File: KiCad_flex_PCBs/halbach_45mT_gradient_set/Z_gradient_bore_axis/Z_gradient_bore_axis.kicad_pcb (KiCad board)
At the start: 2 copper layers, 209.7 x 123 mm, 70 parts, among them J1+ SolderPad, J2- SolderPad

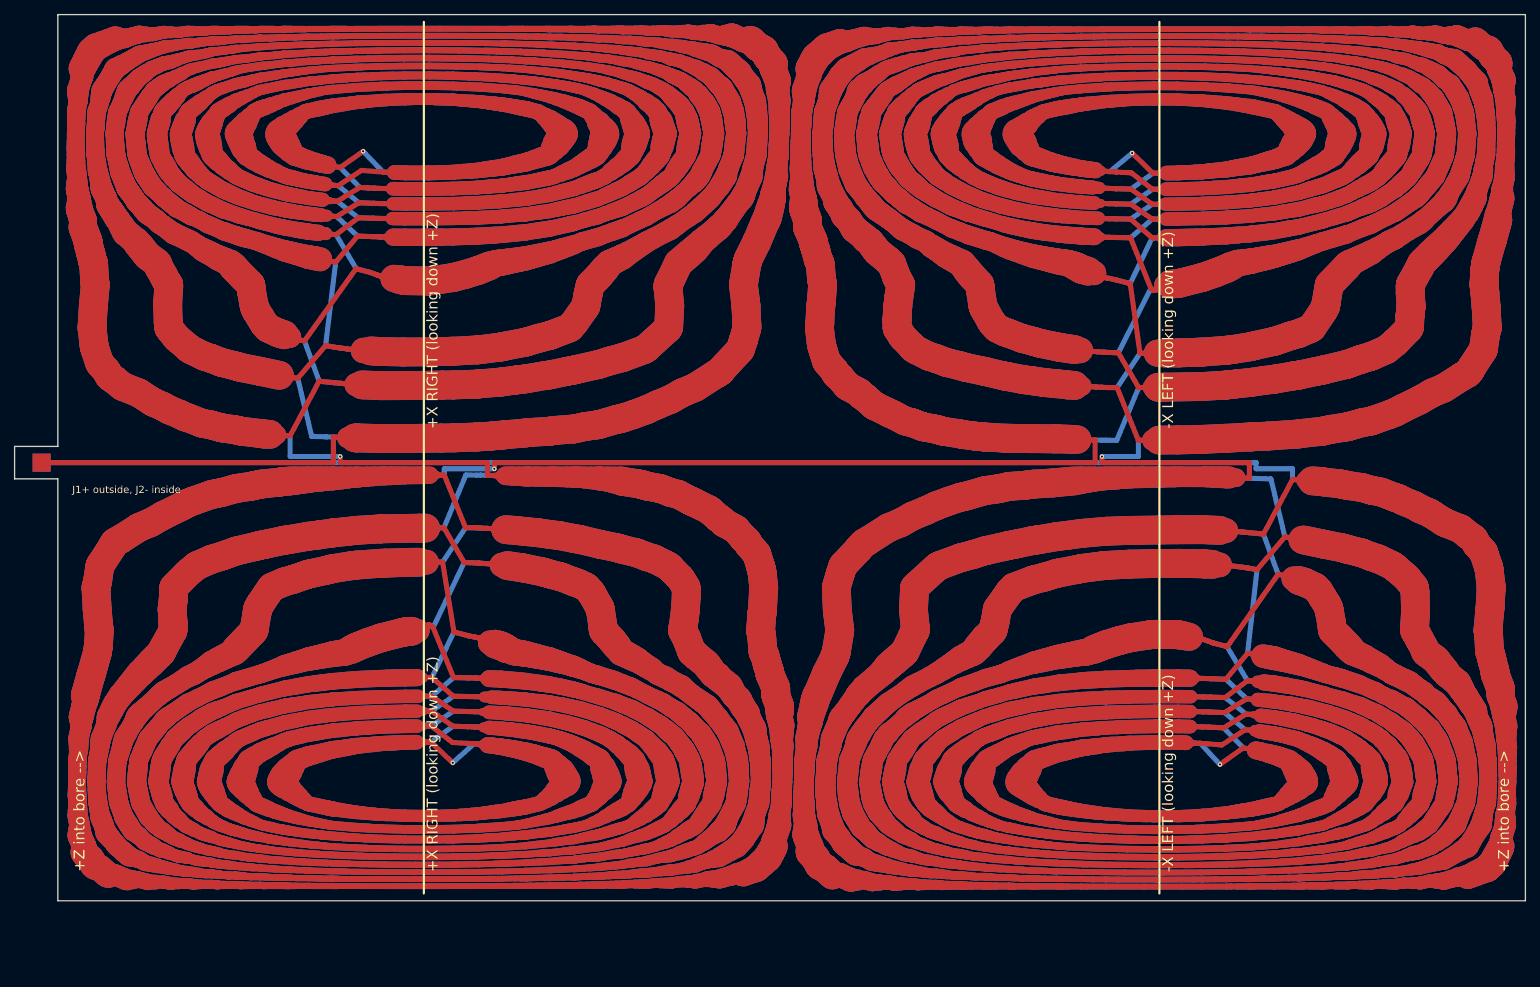
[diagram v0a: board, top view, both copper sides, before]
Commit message: Move the feed tab to the end edge of the flex PCBs
The J1/J2 tab now sticks out past the +axial end of the coil instead of
out of the seam, so the rolled seam is clean and there is room to solder
the leads. Feed and return run as a stacked F.Cu/B.Cu pair along the seam
edge to the routing channel. Larger pads (3 mm) on a 10 mm tab. The tabs
of the three coils sit at their seams: 12, 1 and 6 o'clock looking down +Z.
All boards: DRC clean, same-net gap >= 0.15 mm, re-simulation unchanged.

Co-Authored-By: Claude Opus 5.5 <noreply@anthropic.com>
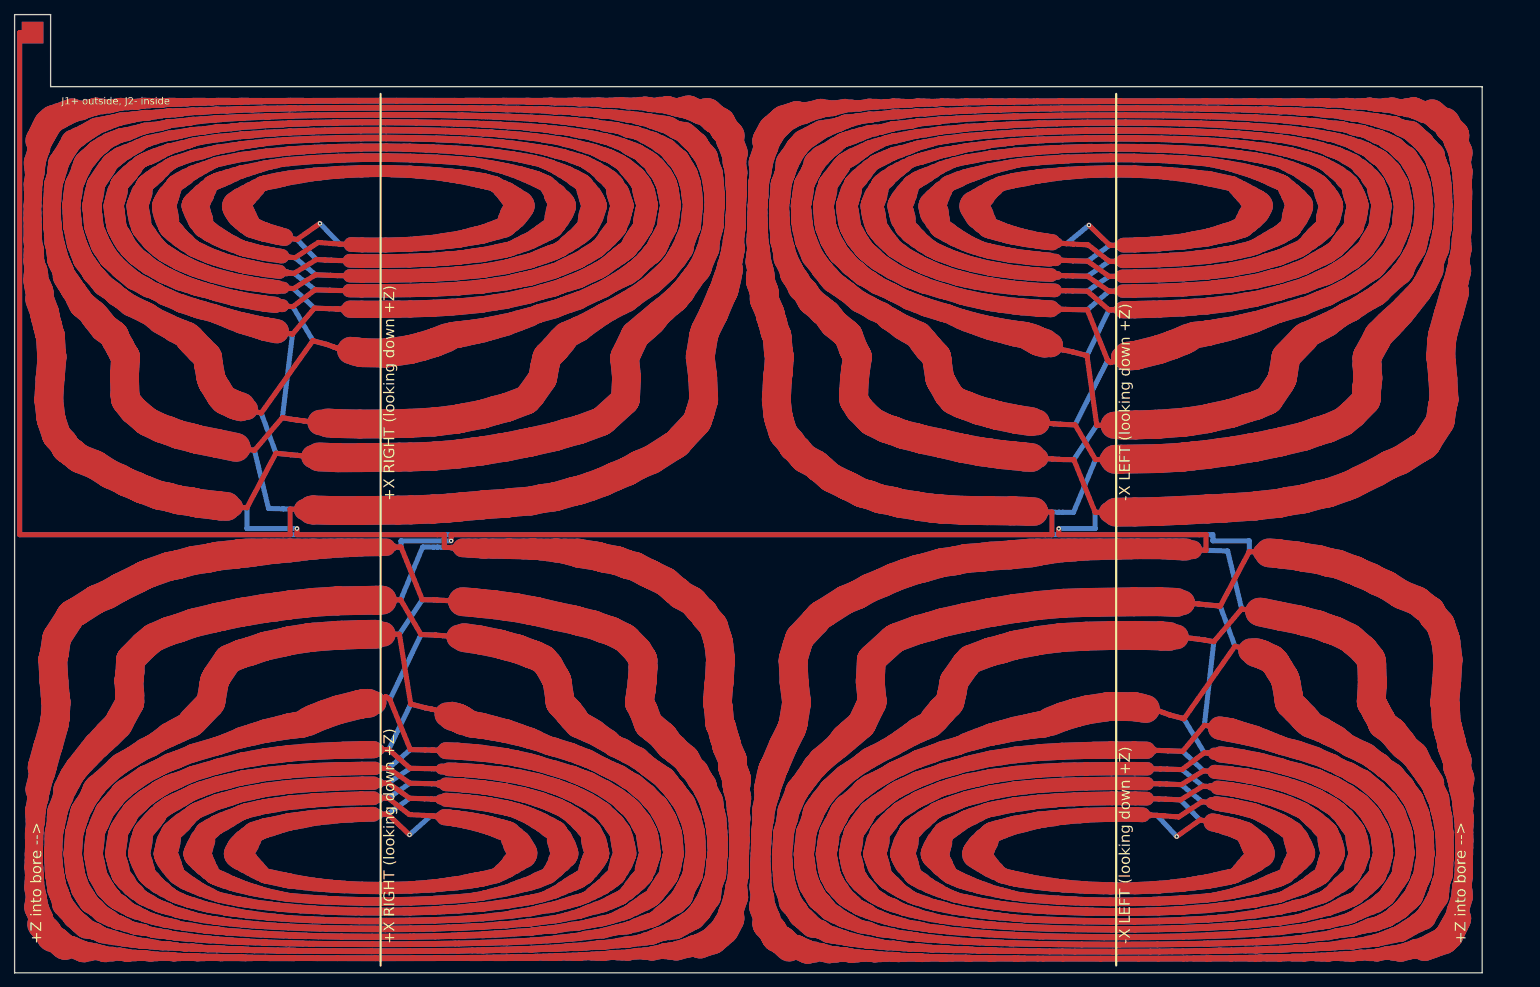
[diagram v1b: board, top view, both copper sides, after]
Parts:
- moved J1+ 59.7 mm to (12.5, 12.5)
- moved J2- 59.7 mm to (12.5, 12.5)
- moved NT37 11.7 mm to (155.2, 66.9)
- moved NT49 11.7 mm to (155.2, 66.9)
- moved NT43 11.7 mm to (157.0, 41.9)
- moved NT9 11.7 mm to (54.2, 41.8)
- moved NT1 11.7 mm to (47.3, 82.2)
- moved NT10 11.7 mm to (54.0, 44.1)
- moved NT11 11.7 mm to (53.8, 46.2)
- moved NT12 11.7 mm to (53.8, 48.3)
- moved NT13 11.7 mm to (53.7, 50.8)
- moved NT14 11.7 mm to (53.4, 55.8)
- moved NT15 11.7 mm to (49.2, 66.3)
- moved NT17 11.7 mm to (47.3, 78.6)
- moved NT18 11.7 mm to (68.7, 82.2)
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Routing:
- net G4_B1: track 446.7 -> 515.3 mm
- net COIL_A: track 39.5 -> 108.1 mm
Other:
- board size 209.7 x 123 mm -> 203.7 x 133 mm

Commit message: Add JLCPCB flex fab profile, stackup, fab checks and board check script
- KiCad_flex_PCBs/fab_profiles/jlcpcb_flex_2layer_1oz_25um_0p2mm.json:
  JLCPCB 2-layer flex (1 oz, 25 um PI, 0.2 mm) stackup, manufacturer
  limits and the design values used.
- export_kicad_flex_pcb 'fab_profile': design values, layer spacing
  (0.06 mm), KiCad stackup (coverlay, Cu, PI, ENIG, 0.2 mm), coverlay
  opening (0.1 mm) and .kicad_pro rules from the profile; every board is
  checked against the limits (report.fab_check).
- check_kicad_flex_pcb / Examples/check_flex_pcb_boards.m: independent
  checks on the board files (KiCad DRC, same-net clearance, manufacturer
  limits, full-width field).
- Boards regenerated: DRC clean, same-net gap >= 0.15 mm, all JLCPCB
  limits met; gradients 7.34 / 19.49 / 18.86 mT/m/A.
- Documentation of the profile and of all checks.

Co-Authored-By: Claude Opus 5.5 <noreply@anthropic.com>
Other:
- rule pad_to_mask_clearance: 0 -> 0.1000
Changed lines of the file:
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@@
 	(generator_version "1.0")
 	(general
-		(thickness 0.11)
+		(thickness 0.2000)
 		(legacy_teardrops no)
 	)
@@
 		(title "Z gradient bore axis")
 		(comment 1 "F.Cu is the outside of the rolled cylinder; J1/J2 on the tab past the end of the coil")
-		(comment 2 "CoilGen mapping: x0=11.2500 y0=81.5000 layer_gap=0.1000")
+		(comment 2 "CoilGen mapping: x0=11.2500 y0=81.5000 layer_gap=0.0600")
 	)
 	(layers
@@
 	)
 	(setup
-		(pad_to_mask_clearance 0)
+		(stackup
+			(layer "F.SilkS"
+				(type "Top Silk Screen")
+			)
+			(layer "F.Mask"
+				(type "Top Solder Mask")
+				(color "Yellow")
+				(thickness 0.0500)
+				(material "Polyimide coverlay (PI 25 um + adhesive 25 um)")
+			)
+			(layer "F.Cu"
+				(type "copper")
+				(thickness 0.0350)
+			)
+			(layer "dielectric 1"
+				(type "core")
+				(thickness 0.0250)
+				(material "Polyimide")
+				(epsilon_r 3.5)
+				(loss_tangent 0.002)
+			)
+			(layer "B.Cu"
+				(type "copper")
+				(thickness 0.0350)
+			)
+			(layer "B.Mask"
+				(type "Bottom Solder Mask")
+				(color "Yellow")
+				(thickness 0.0500)
+				(material "Polyimide coverlay (PI 25 um + adhesive 25 um)")
+			)
+			(layer "B.SilkS"
+				(type "Bottom Silk Screen")
+			)
+			(copper_finish "ENIG")
+			(dielectric_constraints no)
+		)
+		(pad_to_mask_clearance 0.1000)
 		(allow_soldermask_bridges_in_footprints no)
 	)
